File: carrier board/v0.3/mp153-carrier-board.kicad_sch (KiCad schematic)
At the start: 98 parts, among them J1 USB-C_Receptacle_Molex_217179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, J10 3.5mm_Mono_Switched_sm, J11 3.5mm_Mono_Switched_sm, J12 3.5mm_Mono_Switched_sm, J13 3.5mm_Mono_Switched_sm, J2 Eurorack_Power_10pin_Shrouded, J5 3.5mm_Mono_Switched_sm, J9 3.5mm_Mono_Switched_sm, U1 TL072H, U11 TL072H, U12 TL072H, U13 AP6230xZ6, U14 AP2411SN, U3 FUSB302BMPX, U8 TL072H, U9 PCM3060PW

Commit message: carrier board v0.3: finish schematic and PCB
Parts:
- U13: JLCPCB ID (none) -> C1880992
- U2: value ~ -> (none); Display (none) -> MP153-devboard v0.1
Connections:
- net I2C3_SCL is gone; now on net I2C6_SCL: R47.1, U9.1 (MC/SCL/FMT)
- net I2C3_SDA is gone; now on net I2C6_SDA: R48.1, U9.2 (MD/SDA/DEMP)
- net GNDADC: now also U2.B26 (GND_ADC); no longer U2.B28 (V_ADCREF)
- net I2C6_SCL: no longer U2.A3 (PA8)
- net I2C6_SDA: no longer U2.A9 (PC9)
- net VREF+: now also U2.B28 (V_ADCREF); no longer U2.B26 (GND_ADC)
- no-connect marks 47 -> 49
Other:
- note added: "Do not attach VREF+ or GNDADC to clamping diode."
- note added: "Example Audio Codec with Stereo In/Out"
- note added: "Supports DRD (Host or Device mode). Will power attached USB Devices up to ~500mA. This circuit will not allow powering the mp153 board via the USB jack (to do that, an additional AP2411 is needed)"
- note added: "Use low-offset op-amp with series 68 ohm resistor on all ADC inputs, to reduce time required to measure each ADC channel."
- note removed: "Example Audio Codec + Stereo In/Out"
- note removed: "Note: Do not attach VREF+ or GNDADC to clamping diode."
- note removed: "Note: Use op-amp with series 68 ohm resistor on all ADC inputs, to reduce time required to measure each ADC channel."
- note removed: "~300mA of +5V required, plus up to 500mA more if powering USB devices"
- moved on the sheet: R47, R48

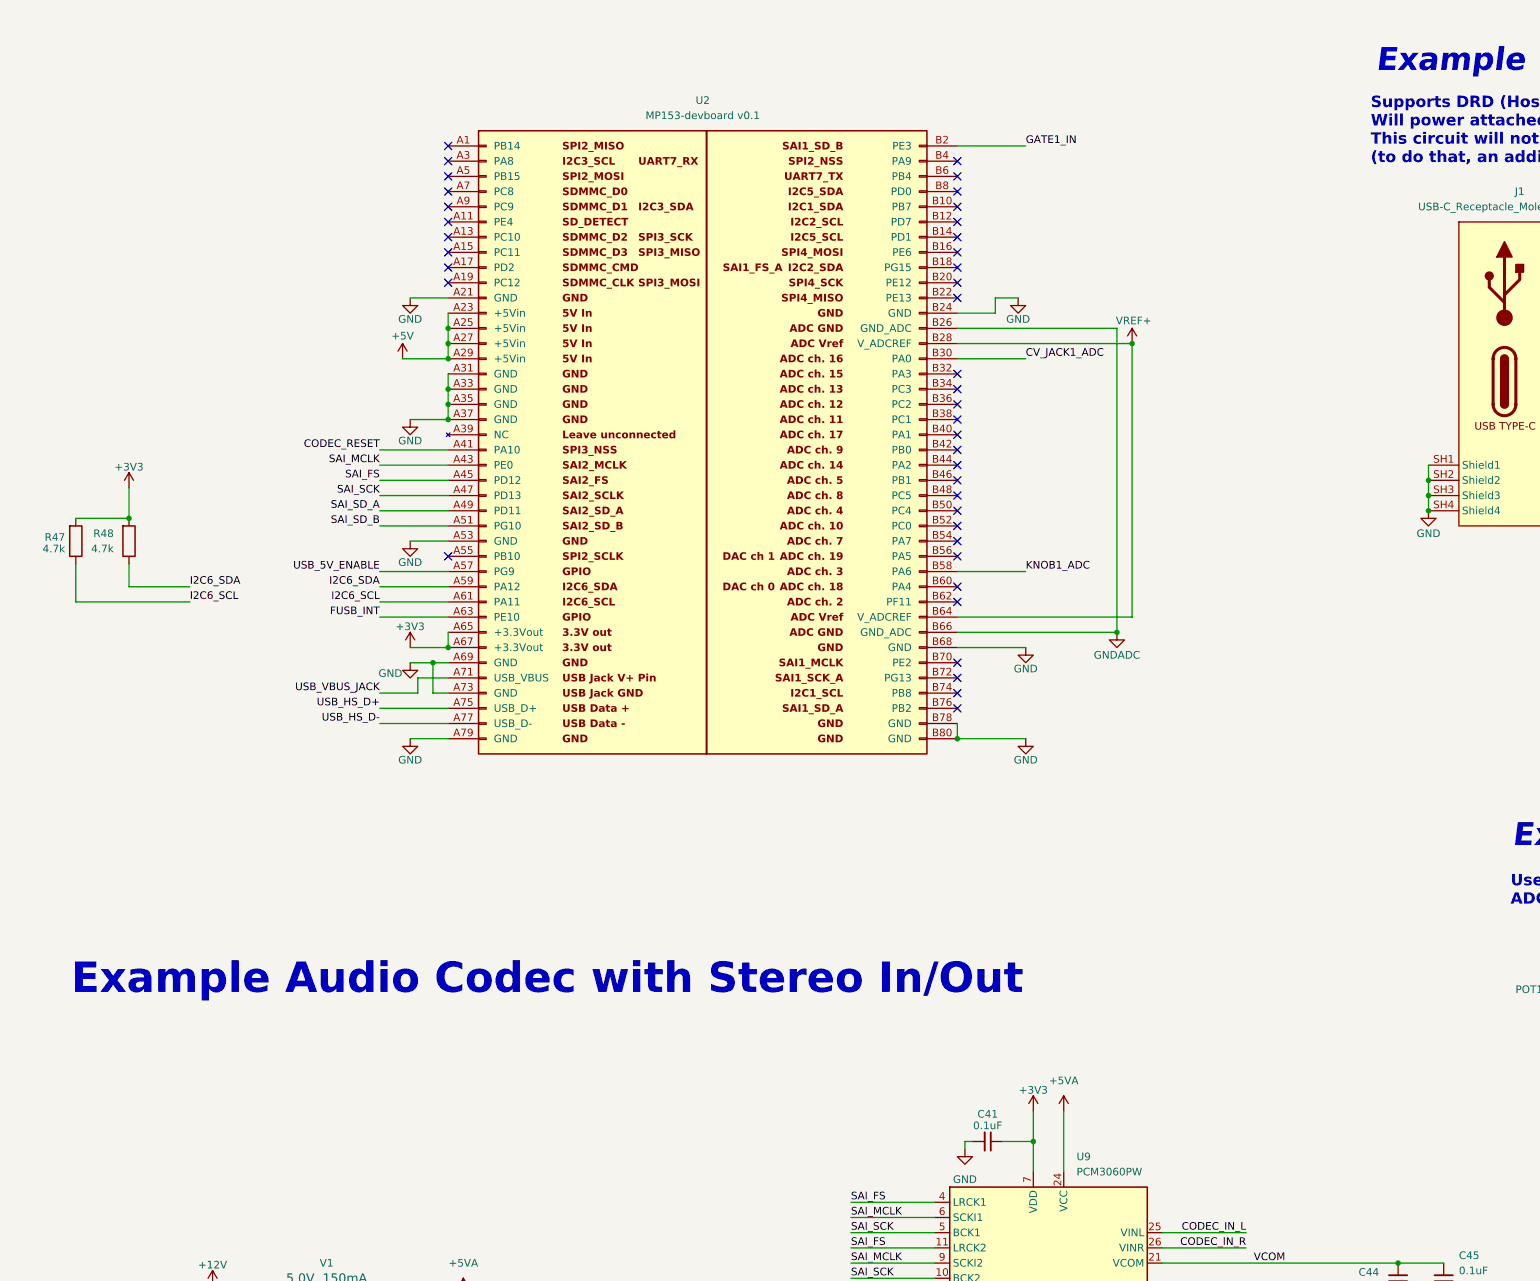
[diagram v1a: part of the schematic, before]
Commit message: JLC Producton files for carrier board v0.3
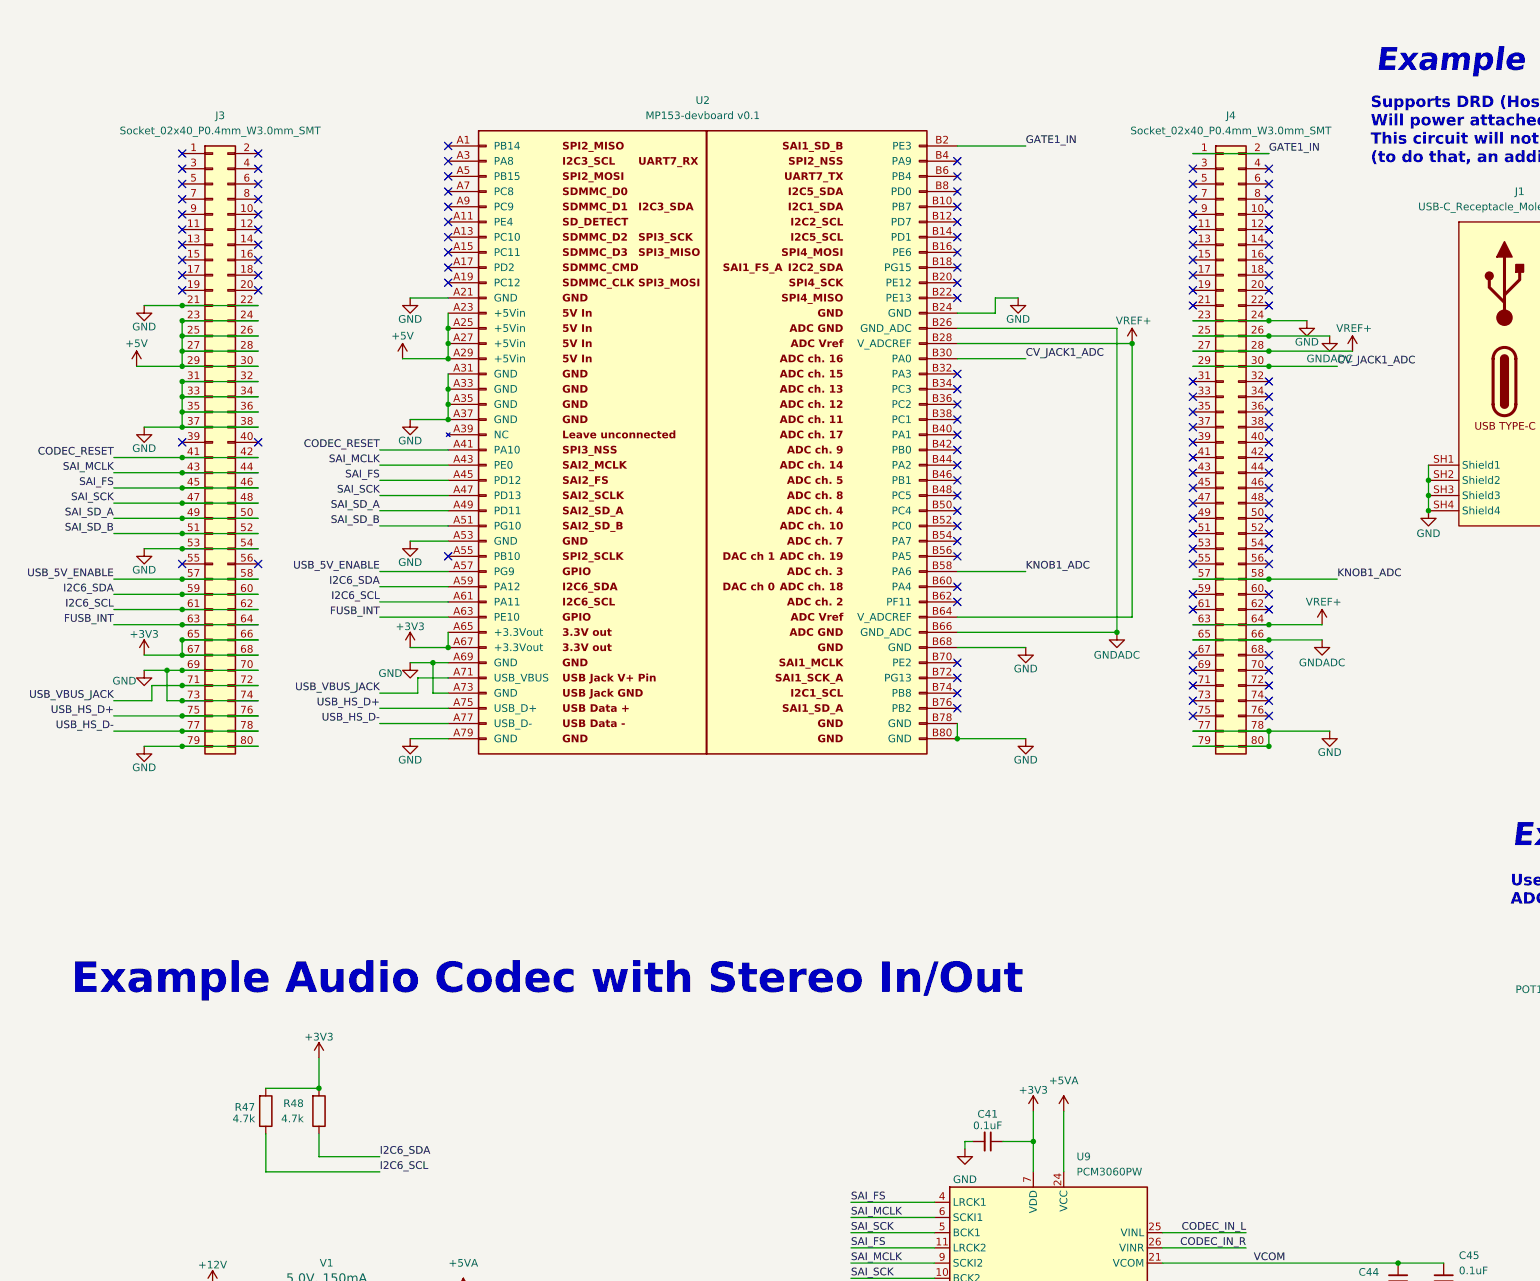
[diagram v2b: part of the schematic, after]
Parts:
- added J3, J4: Socket_02x40_P0.4mm_W3.0mm_SMT, mp153-devboard:Connector-80socket-P0.4mm-W3.0mm, symbol 4ms_Connector:Socket_02x40_P0.4mm_W3.0mm_SMT
- U2: value (none) -> ~
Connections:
- net +3V3: now also J3.65 (Pin_65), J3.66 (Pin_66), J3.67 (Pin_67), J3.68 (Pin_68)
- net +5V: now also J3.23 (Pin_23), J3.24 (Pin_24), J3.25 (Pin_25), J3.26 (Pin_26), J3.27 (Pin_27), J3.28 (Pin_28), J3.29 (Pin_29), J3.30 (Pin_30)
- net CODEC_RESET: now also J3.41 (Pin_41), J3.42 (Pin_42)
- net CV_JACK1_ADC: now also J4.29 (Pin_29), J4.30 (Pin_30)
- net FUSB_INT: now also J3.63 (Pin_63), J3.64 (Pin_64)
- net GATE1_IN: now also J4.1 (Pin_1), J4.2 (Pin_2)
- net GND: now also J3.21 (Pin_21), J3.22 (Pin_22), J3.31 (Pin_31), J3.32 (Pin_32), J3.33 (Pin_33), J3.34 (Pin_34), J3.35 (Pin_35), J3.36 (Pin_36), J3.37 (Pin_37), J3.38 (Pin_38), J3.53 (Pin_53), J3.54 (Pin_54), J3.69 (Pin_69), J3.70 (Pin_70), J3.73 (Pin_73), J3.74 (Pin_74), J3.79 (Pin_79), J3.80 (Pin_80), J4.23 (Pin_23), J4.24 (Pin_24), J4.77 (Pin_77), J4.78 (Pin_78), J4.79 (Pin_79), J4.80 (Pin_80)
- net GNDADC: now also J4.25 (Pin_25), J4.26 (Pin_26), J4.65 (Pin_65), J4.66 (Pin_66)
- net I2C6_SCL: now also J3.61 (Pin_61), J3.62 (Pin_62)
- net I2C6_SDA: now also J3.59 (Pin_59), J3.60 (Pin_60)
- net KNOB1_ADC: now also J4.57 (Pin_57), J4.58 (Pin_58)
- net SAI_FS: now also J3.45 (Pin_45), J3.46 (Pin_46)
- net SAI_MCLK: now also J3.43 (Pin_43), J3.44 (Pin_44)
- net SAI_SCK: now also J3.47 (Pin_47), J3.48 (Pin_48)
- net SAI_SD_A: now also J3.49 (Pin_49), J3.50 (Pin_50)
- net SAI_SD_B: now also J3.51 (Pin_51), J3.52 (Pin_52)
- net USB_5V_ENABLE: now also J3.57 (Pin_57), J3.58 (Pin_58)
- net USB_HS_D+: now also J3.75 (Pin_75), J3.76 (Pin_76)
- net USB_HS_D-: now also J3.77 (Pin_77), J3.78 (Pin_78)
- net USB_VBUS_JACK: now also J3.71 (Pin_71), J3.72 (Pin_72)
- net VREF+: now also J4.27 (Pin_27), J4.28 (Pin_28), J4.63 (Pin_63), J4.64 (Pin_64)
- no-connect marks 49 -> 133
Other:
- moved on the sheet: R47, R48
